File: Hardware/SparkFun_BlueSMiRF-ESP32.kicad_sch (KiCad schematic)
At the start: 27 parts, among them J2 Conn_01x06, Q1 Q_NMOS_DGS, Q2 Q_NMOS_DGS, SW1 Switch, U1 ESP32_Pico_Mini, U2 AP2112K-3.3

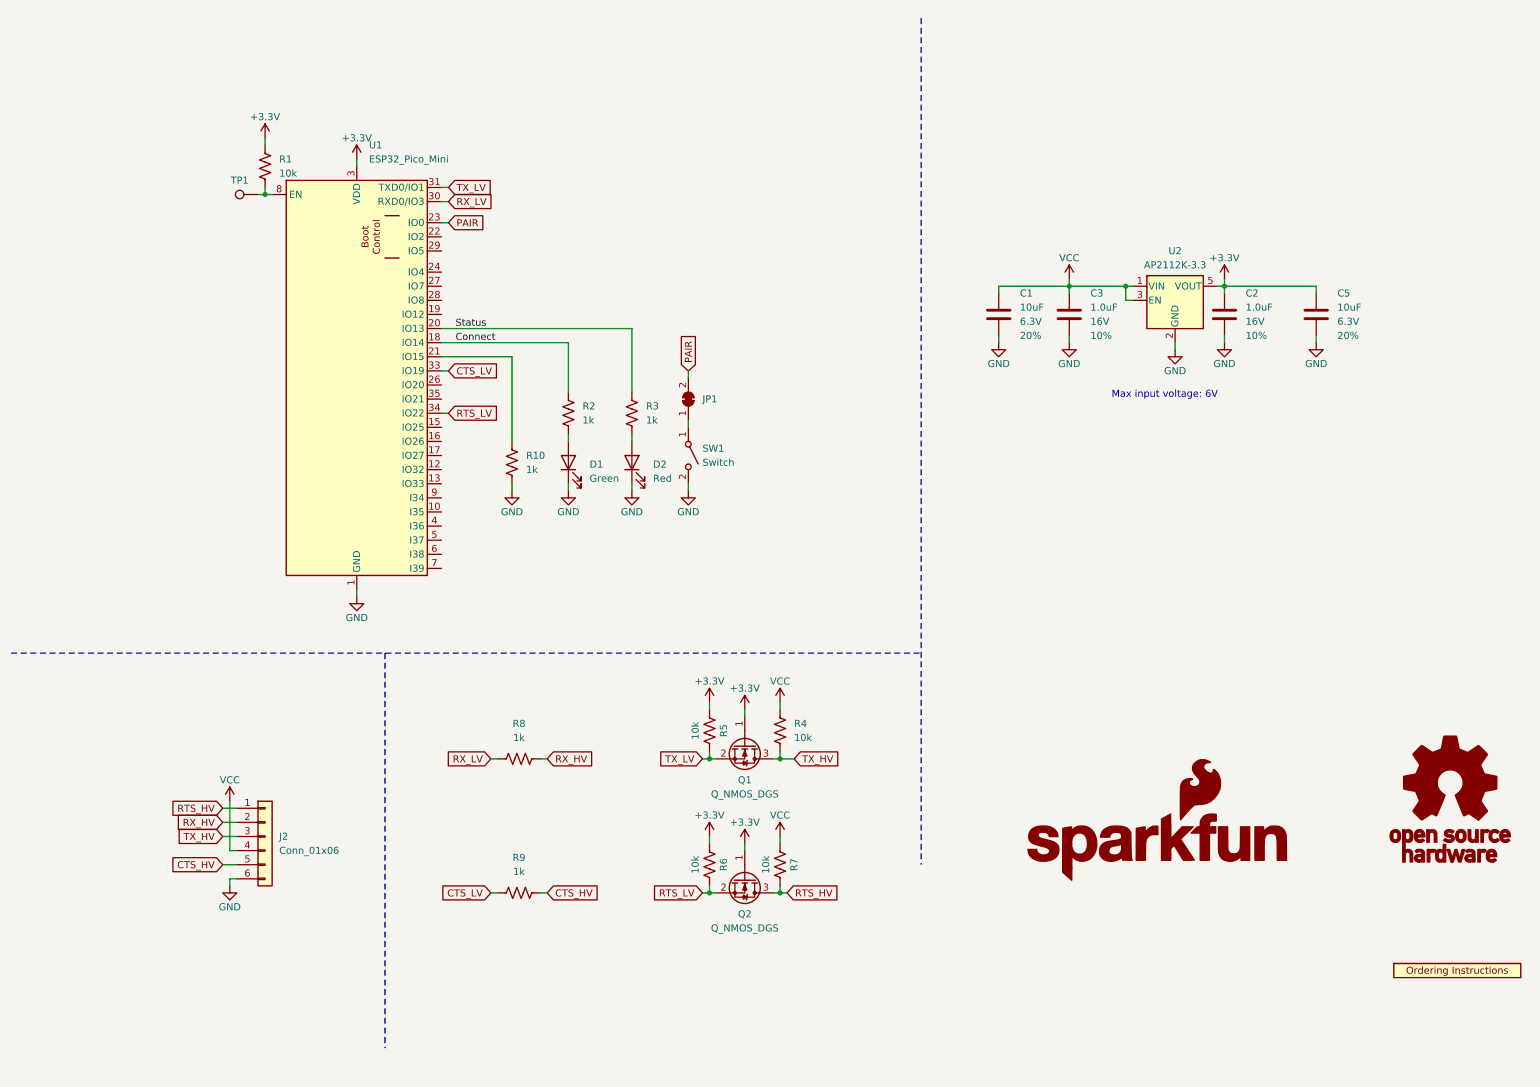
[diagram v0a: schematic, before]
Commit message: Update panel with PROD_IDs.
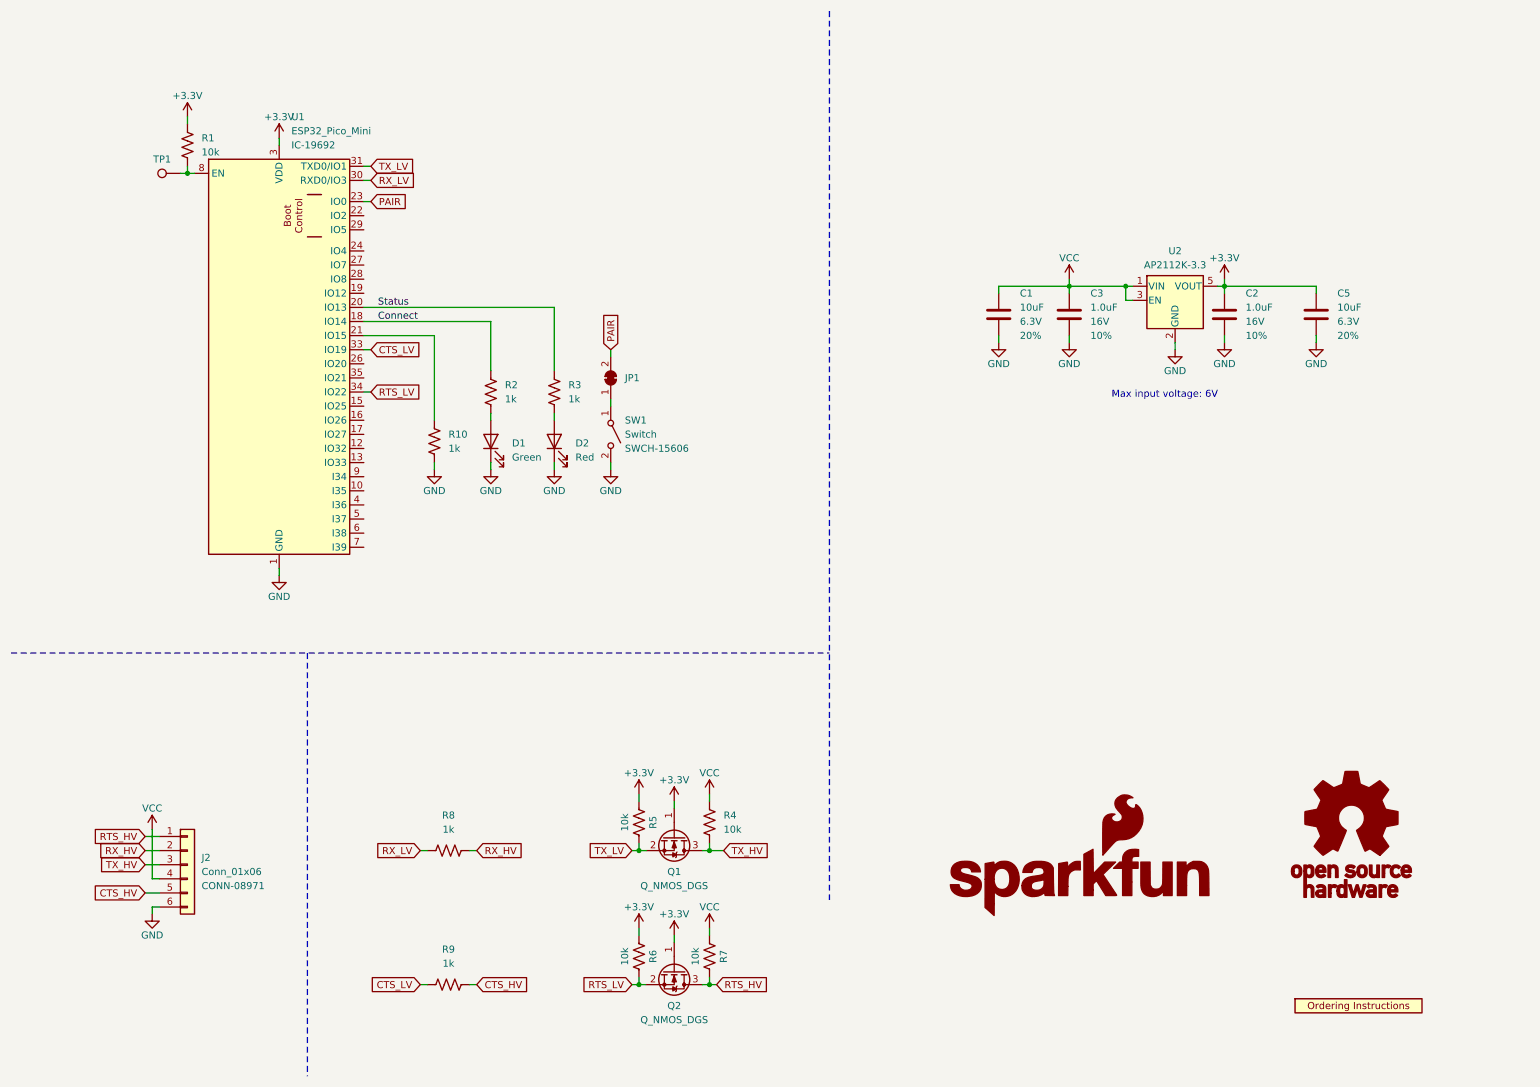
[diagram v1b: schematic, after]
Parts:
- J2: PROD_ID (none) -> CONN-08971
- SW1: symbol SparkFun-Switch:Momentary_4.6x2.8mm -> SparkFun-Switch:SPST_Momentary_4.6x2.8mm; PROD_ID (none) -> SWCH-15606
- U1: symbol SparkFun-RF:ESP32_Pico_Mini -> SparkFun-RF:ESP32-PICO-V3-02; PROD_ID (none) -> IC-19692
- U2: PROD_ID (none) -> VREG-12457
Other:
- title: BlueSMiRF -> BlueSMiRF - ESP32
- moved on the sheet: D1, D2, J2, JP1, Q1, Q2, R1, R10, R2, R3, R4, R5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

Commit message: Update PROD_IDs
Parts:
- C1, C5: PROD_ID 11015 -> CAP-11015
- C2, C3: PROD_ID 13930 -> CAP-13930
- D1: PROD_ID 821 -> DIO-00821
- D2: PROD_ID 819 -> DIO-00819
- Q1, Q2: PROD_ID 830 -> TRANS-00830
- R1, R4, R5, R6, R7: PROD_ID 824 -> RES-00824
- R10, R2, R3, R8, R9: PROD_ID 7856 -> RES-07856
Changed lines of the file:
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@@
       (effects (font (size 1.27 1.27)) hide)
     )
-    (property "Datasheet" "~" (at 99.06 88.9 0)
-      (effects (font (size 1.27 1.27)) hide)
-    )
-    (property "PROD_ID" "821" (at 104.394 89.154 0)
+    (property "Datasheet" "https://docs.broadcom.com/docs/AV02-0551EN" (at 99.06 88.9 0)
+      (effects (font (size 1.27 1.27)) hide)
+    )
+    (property "PROD_ID" "DIO-00821" (at 104.394 89.154 0)
       (effects (font (size 1.27 1.27)) hide)
     )
@@
       (effects (font (size 1.27 1.27)) hide)
     )
-    (property "Datasheet" "~" (at 231.14 66.04 0)
-      (effects (font (size 1.27 1.27)) hide)
-    )
-    (property "PROD_ID" "13930" (at 227.33 68.58 0)
+    (property "Datasheet" "[link text](https://cdn.sparkfun.com/assets/8/a/4/a/5/Kemet_Capacitor_Datasheet.pdf)" (at 231.14 66.04 0)
+      (effects (font (size 1.27 1.27)) hide)
+    )
+    (property "PROD_ID" "CAP-13930" (at 227.33 68.58 0)
       (effects (font (size 1.27 1.27)) hide)
     )
@@
       (effects (font (size 1.27 1.27)) hide)
     )
-    (property "Datasheet" "~" (at 125.73 157.48 0)
-      (effects (font (size 1.27 1.27)) hide)
-    )
-    (property "PROD_ID" "824" (at 132.08 157.48 90)
+    (property "Datasheet" "https://www.vishay.com/docs/20035/dcrcwe3.pdf" (at 125.73 157.48 0)
+      (effects (font (size 1.27 1.27)) hide)
+    )
+    (property "PROD_ID" "RES-00824" (at 132.08 157.48 90)
       (effects (font (size 1.27 1.27)) hide)
     )
@@
       (effects (font (size 1.27 1.27)) hide)
     )
-    (property "Datasheet" "~" (at 91.44 162.56 0)
-      (effects (font (size 1.27 1.27)) hide)
-    )
-    (property "PROD_ID" "7856" (at 91.44 155.702 90)
+    (property "Datasheet" "https://www.vishay.com/docs/20035/dcrcwe3.pdf" (at 91.44 162.56 0)
+      (effects (font (size 1.27 1.27)) hide)
+    )
+    (property "PROD_ID" "RES-07856" (at 91.44 155.702 90)
       (effects (font (size 1.27 1.27)) hide)
     )
@@
       (effects (font (size 1.27 1.27)) hide)
     )
-    (property "Datasheet" "~" (at 190.5 66.04 0)
-      (effects (font (size 1.27 1.27)) hide)
-    )
-    (property "PROD_ID" "11015" (at 186.69 68.58 0)
+    (property "Datasheet" "[link text](https://cdn.sparkfun.com/assets/8/a/4/a/5/Kemet_Capacitor_Datasheet.pdf)" (at 190.5 66.04 0)
+      (effects (font (size 1.27 1.27)) hide)
+    )
+    (property "PROD_ID" "CAP-11015" (at 186.69 68.58 0)
       (effects (font (size 1.27 1.27)) hide)
     )
@@
       (effects (font (size 1.27 1.27)) hide)
     )
-    (property "PROD_ID" "830" (at 132.08 160.02 0)
+    (property "PROD_ID" "TRANS-00830" (at 132.08 160.02 0)
       (effects (font (size 1.27 1.27)) hide)
     )
@@
       (effects (font (size 1.27 1.27)) hide)
     )
-    (property "Datasheet" "~" (at 203.2 66.04 0)
-      (effects (font (size 1.27 1.27)) hide)
-    )
-    (property "PROD_ID" "13930" (at 199.39 68.58 0)
+    (property "Datasheet" "[link text](https://cdn.sparkfun.com/assets/8/a/4/a/5/Kemet_Capacitor_Datasheet.pdf)" (at 203.2 66.04 0)
+      (effects (font (size 1.27 1.27)) hide)
+    )
+    (property "PROD_ID" "CAP-13930" (at 199.39 68.58 0)
       (effects (font (size 1.27 1.27)) hide)
     )
@@
     )
     (property "PROD_ID" "SWCH-15606" (at 123.19 90.17 90)
-      (effects (font (size 1.27 1.27)) (justify left))
+      (effects (font (size 1.27 1.27)) (justify left) hide)
     )
     (pin "1")
@@
       (effects (font (size 1.27 1.27)) hide)
     )
-    (property "Datasheet" "~" (at 99.06 80.01 0)
-      (effects (font (size 1.27 1.27)) hide)
-    )
-    (property "PROD_ID" "7856" (at 105.918 80.01 90)
+    (property "Datasheet" "https://www.vishay.com/docs/20035/dcrcwe3.pdf" (at 99.06 80.01 0)
+      (effects (font (size 1.27 1.27)) hide)
+    )
+    (property "PROD_ID" "RES-07856" (at 105.918 80.01 90)
       (effects (font (size 1.27 1.27)) hide)
     )
@@
       (effects (font (size 1.27 1.27)) hide)
     )
-    (property "Datasheet" "~" (at 91.44 186.69 0)
-      (effects (font (size 1.27 1.27)) hide)
-    )
-    (property "PROD_ID" "7856" (at 91.44 179.832 90)
+    (property "Datasheet" "https://www.vishay.com/docs/20035/dcrcwe3.pdf" (at 91.44 186.69 0)
+      (effects (font (size 1.27 1.27)) hide)
+    )
+    (property "PROD_ID" "RES-07856" (at 91.44 179.832 90)
       (effects (font (size 1.27 1.27)) hide)
     )
@@
       (effects (font (size 1.27 1.27)) hide)
     )
-    (property "PROD_ID" "830" (at 132.08 184.15 0)
+    (property "PROD_ID" "TRANS-00830" (at 132.08 184.15 0)
       (effects (font (size 1.27 1.27)) hide)
     )
@@
       (effects (font (size 1.27 1.27)) hide)
     )
-    (property "Datasheet" "~" (at 247.65 66.04 0)
-      (effects (font (size 1.27 1.27)) hide)
-    )
-    (property "PROD_ID" "11015" (at 243.84 68.58 0)
+    (property "Datasheet" "[link text](https://cdn.sparkfun.com/assets/8/a/4/a/5/Kemet_Capacitor_Datasheet.pdf)" (at 247.65 66.04 0)
+      (effects (font (size 1.27 1.27)) hide)
+    )
+    (property "PROD_ID" "CAP-11015" (at 243.84 68.58 0)
       (effects (font (size 1.27 1.27)) hide)
     )
@@
       (effects (font (size 1.27 1.27)) hide)
     )
-    (property "Datasheet" "~" (at 110.49 80.01 0)
-      (effects (font (size 1.27 1.27)) hide)
-    )
-    (property "PROD_ID" "7856" (at 117.348 80.01 90)
+    (property "Datasheet" "https://www.vishay.com/docs/20035/dcrcwe3.pdf" (at 110.49 80.01 0)
+      (effects (font (size 1.27 1.27)) hide)
+    )
+    (property "PROD_ID" "RES-07856" (at 117.348 80.01 90)
       (effects (font (size 1.27 1.27)) hide)
     )
@@
       (effects (font (size 1.27 1.27)) hide)
     )
-    (property "Datasheet" "~" (at 44.45 165.1 0)
+    (property "Datasheet" "https://www.sparkfun.com/datasheets/Prototyping/Connectors/11029.pdf" (at 44.45 165.1 0)
       (effects (font (size 1.27 1.27)) hide)
     )
     (property "PROD_ID" "CONN-08971" (at 46.99 168.91 0)
-      (effects (font (size 1.27 1.27)) (justify left))
+      (effects (font (size 1.27 1.27)) (justify left) hide)
     )
     (pin "1")
@@
       (effects (font (size 1.27 1.27)) hide)
     )
-    (property "Datasheet" "~" (at 138.43 157.48 0)
-      (effects (font (size 1.27 1.27)) hide)
-    )
-    (property "PROD_ID" "824" (at 144.78 157.48 90)
+    (property "Datasheet" "https://www.vishay.com/docs/20035/dcrcwe3.pdf" (at 138.43 157.48 0)
+      (effects (font (size 1.27 1.27)) hide)
+    )
+    (property "PROD_ID" "RES-00824" (at 144.78 157.48 90)
       (effects (font (size 1.27 1.27)) hide)
     )
@@
       (effects (font (size 1.27 1.27)) hide)
     )
-    (property "Datasheet" "~" (at 88.9 88.9 0)
-      (effects (font (size 1.27 1.27)) hide)
-    )
-    (property "PROD_ID" "7856" (at 95.758 88.9 90)
+    (property "Datasheet" "https://www.vishay.com/docs/20035/dcrcwe3.pdf" (at 88.9 88.9 0)
+      (effects (font (size 1.27 1.27)) hide)
+    )
+    (property "PROD_ID" "RES-07856" (at 95.758 88.9 90)
       (effects (font (size 1.27 1.27)) hide)
     )
@@
       (effects (font (size 1.27 1.27)) hide)
     )
-    (property "Datasheet" "~" (at 110.49 88.9 0)
-      (effects (font (size 1.27 1.27)) hide)
-    )
-    (property "PROD_ID" "819" (at 115.062 88.9 0)
+    (property "Datasheet" "https://docs.broadcom.com/docs/AV02-0551EN" (at 110.49 88.9 0)
+      (effects (font (size 1.27 1.27)) hide)
+    )
+    (property "PROD_ID" "DIO-00819" (at 115.062 88.9 0)
       (effects (font (size 1.27 1.27)) hide)
     )
@@
       (effects (font (size 1.27 1.27)) hide)
     )
-    (property "Datasheet" "~" (at 125.73 181.61 0)
-      (effects (font (size 1.27 1.27)) hide)
-    )
-    (property "PROD_ID" "824" (at 132.08 181.61 90)
+    (property "Datasheet" "https://www.vishay.com/docs/20035/dcrcwe3.pdf" (at 125.73 181.61 0)
+      (effects (font (size 1.27 1.27)) hide)
+    )
+    (property "PROD_ID" "RES-00824" (at 132.08 181.61 90)
       (effects (font (size 1.27 1.27)) hide)
     )
@@
       (effects (font (size 1.27 1.27)) hide)
     )
-    (property "Datasheet" "~" (at 138.43 181.61 0)
-      (effects (font (size 1.27 1.27)) hide)
-    )
-    (property "PROD_ID" "824" (at 144.78 181.61 90)
+    (property "Datasheet" "https://www.vishay.com/docs/20035/dcrcwe3.pdf" (at 138.43 181.61 0)
+      (effects (font (size 1.27 1.27)) hide)
+    )
+    (property "PROD_ID" "RES-00824" (at 144.78 181.61 90)
       (effects (font (size 1.27 1.27)) hide)
     )
@@
       (effects (font (size 1.27 1.27)) hide)
     )
-    (property "Datasheet" "~" (at 44.45 35.56 0)
-      (effects (font (size 1.27 1.27)) hide)
-    )
-    (property "PROD_ID" "824" (at 50.8 35.56 90)
-      (effects (font (size 1.27 1.27)) hide)
-    )
+    (property "Datasheet" "https://www.vishay.com/docs/20035/dcrcwe3.pdf" (at 44.45 35.56 0)
+      (effects (font (size 1.27 1.27)) hide)
+    )
+    (property "PROD_ID" "RES-00824" (at 50.8 35.56 90)
+      (effects (font (size 1.27 1.27)) hide)
+    )
